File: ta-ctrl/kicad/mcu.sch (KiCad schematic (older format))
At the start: 5 parts

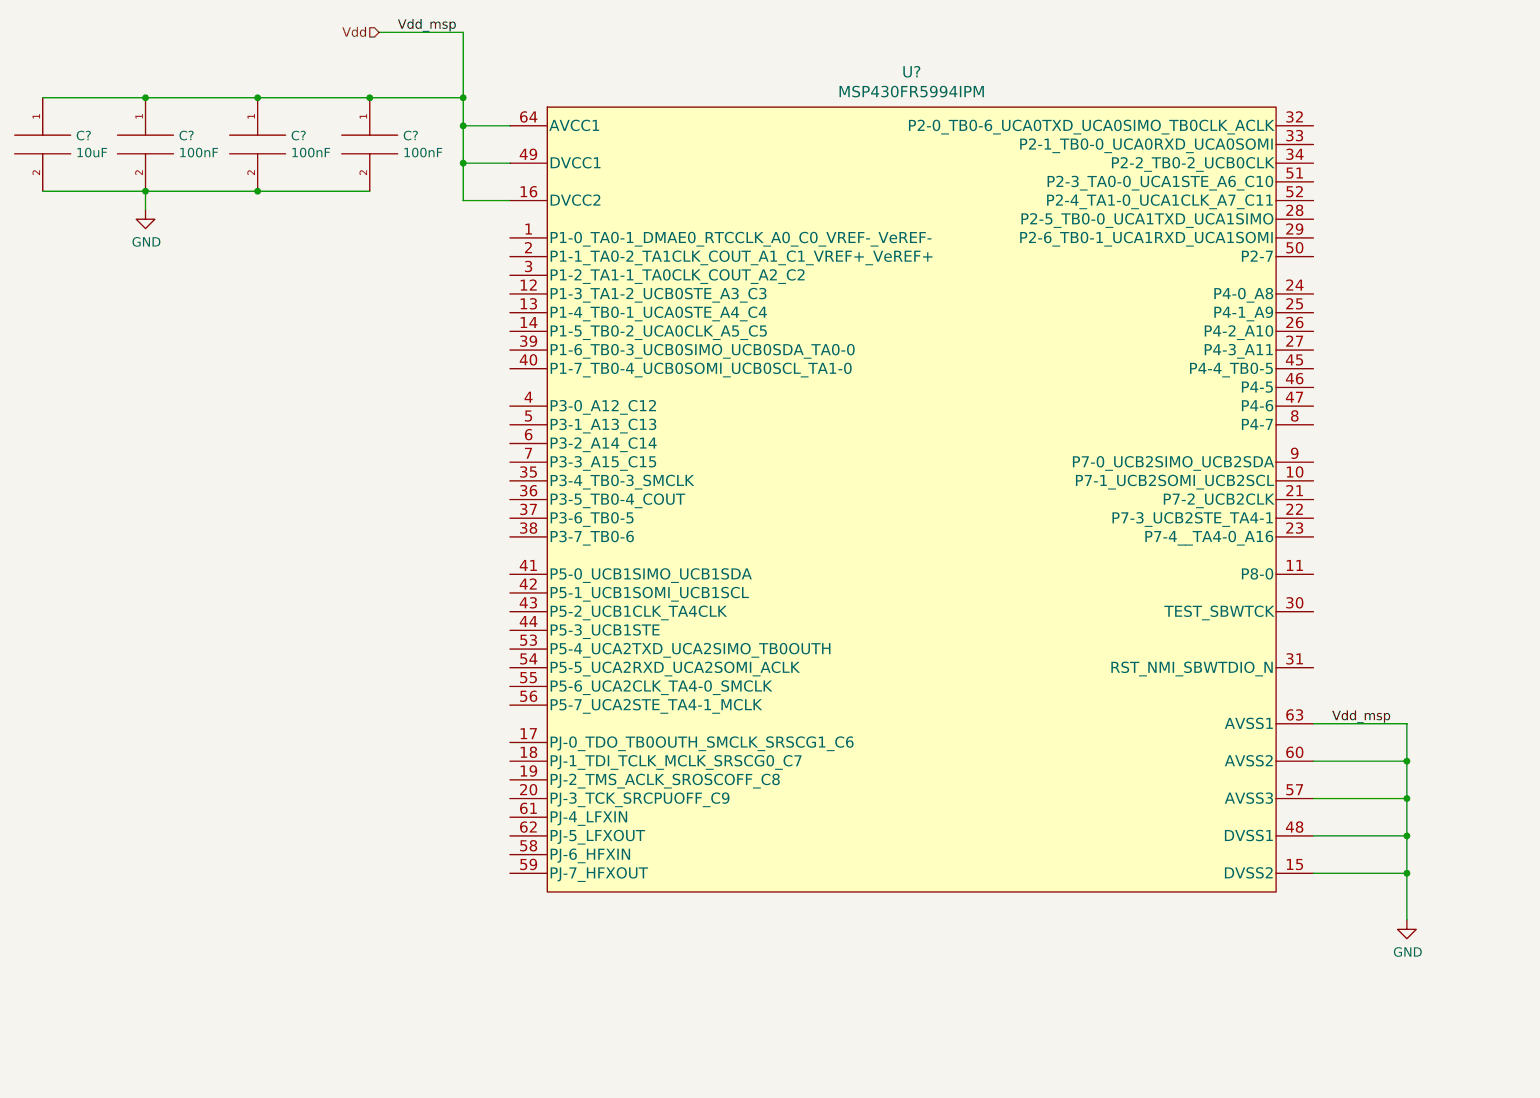
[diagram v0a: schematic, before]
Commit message: Added initial pin assignments
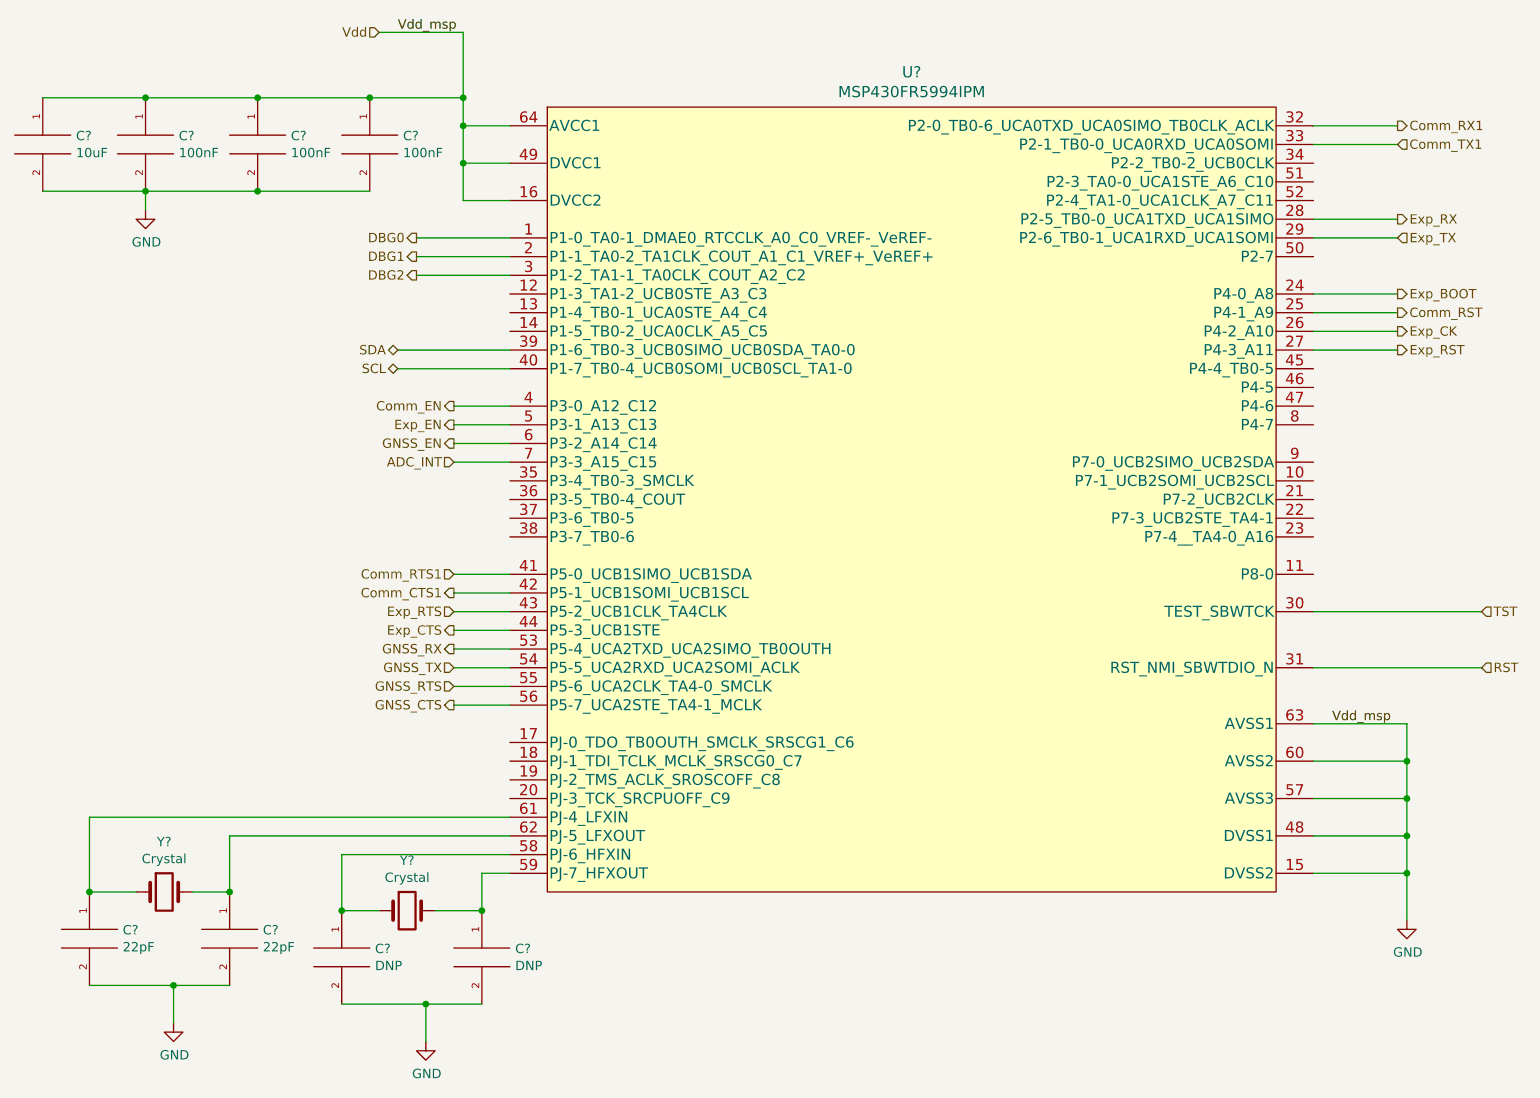
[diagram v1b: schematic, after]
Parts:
- added C? (x2): 22pF, symbol pspice:C
- added C? (x2): DNP, symbol pspice:C
- added Y? (x2): Crystal, symbol Device:Crystal
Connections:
- net GND: now also C?.2, C?.2, C?.2, C?.2
- net DBG0: now reaches U?.1 (P1-0_TA0-1_DMAE0_RTCCLK_A0_C0_VREF-_VeREF-)
- net DBG1: now reaches U?.2 (P1-1_TA0-2_TA1CLK_COUT_A1_C1_VREF+_VeREF+)
- net Exp_BOOT: now reaches U?.24 (P4-0_A8)
- net Comm_RST: now reaches U?.25 (P4-1_A9)
- net Exp_CK: now reaches U?.26 (P4-2_A10)
- net Exp_RST: now reaches U?.27 (P4-3_A11)
- net Exp_RX: now reaches U?.28 (P2-5_TB0-0_UCA1TXD_UCA1SIMO)
- net Exp_TX: now reaches U?.29 (P2-6_TB0-1_UCA1RXD_UCA1SOMI)
- net DBG2: now reaches U?.3 (P1-2_TA1-1_TA0CLK_COUT_A2_C2)
- net TST: now reaches U?.30 (TEST_SBWTCK)
- net RST: now reaches U?.31 (RST_NMI_SBWTDIO_N)
- net Comm_RX1: now reaches U?.32 (P2-0_TB0-6_UCA0TXD_UCA0SIMO_TB0CLK_ACLK)
- net Comm_TX1: now reaches U?.33 (P2-1_TB0-0_UCA0RXD_UCA0SOMI)
- net SDA: now reaches U?.39 (P1-6_TB0-3_UCB0SIMO_UCB0SDA_TA0-0)
- net Comm_EN: now reaches U?.4 (P3-0_A12_C12)
- net SCL: now reaches U?.40 (P1-7_TB0-4_UCB0SOMI_UCB0SCL_TA1-0)
- net Comm_RTS1: now reaches U?.41 (P5-0_UCB1SIMO_UCB1SDA)
- net Comm_CTS1: now reaches U?.42 (P5-1_UCB1SOMI_UCB1SCL)
- net Exp_RTS: now reaches U?.43 (P5-2_UCB1CLK_TA4CLK)
- net Exp_CTS: now reaches U?.44 (P5-3_UCB1STE)
- net Exp_EN: now reaches U?.5 (P3-1_A13_C13)
- net GNSS_RX: now reaches U?.53 (P5-4_UCA2TXD_UCA2SIMO_TB0OUTH)
- net GNSS_TX: now reaches U?.54 (P5-5_UCA2RXD_UCA2SOMI_ACLK)
- net GNSS_RTS: now reaches U?.55 (P5-6_UCA2CLK_TA4-0_SMCLK)
- net GNSS_CTS: now reaches U?.56 (P5-7_UCA2STE_TA4-1_MCLK)
- net at U?.58 (PJ-6_HFXIN): now also C?.1, Y?.1
- net at U?.59 (PJ-7_HFXOUT): now also C?.1, Y?.2
- net GNSS_EN: now reaches U?.6 (P3-2_A14_C14)
- net at U?.61 (PJ-4_LFXIN): now also C?.1, Y?.1
- net at U?.62 (PJ-5_LFXOUT): now also C?.1, Y?.2
- net ADC_INT: now reaches U?.7 (P3-3_A15_C15)
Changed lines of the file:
@@
 	3100 1750 3350 1750
-Wire Wire Line
-	3100 1750 3100 1950
-Wire Wire Line
-	3100 1950 3350 1950
-Connection ~ 3100 1750
 Wire Wire Line
 	3100 1550 3100 1400
@@
 Wire Wire Line
 	850  1900 1400 1900
+$Comp
+L Device:Crystal Y?
+U 1 1 5F187D6E
+P 2800 5750
+F 0 "Y?" H 2800 6018 50  0000 C CNN
+F 1 "Crystal" H 2800 5927 50  0000 C CNN
+F 2 "" H 2800 5750 50  0001 C CNN
+F 3 "~" H 2800 5750 50  0001 C CNN
+	1    2800 5750
+	1    0    0    -1
+$EndComp
+$Comp
+L Device:Crystal Y?
+U 1 1 5F18970C
+P 1500 5650
+F 0 "Y?" H 1500 5918 50  0000 C CNN
+F 1 "Crystal" H 1500 5827 50  0000 C CNN
+F 2 "" H 1500 5650 50  0001 C CNN
+F 3 "~" H 1500 5650 50  0001 C CNN
+	1    1500 5650
+	1    0    0    -1
+$EndComp
+$Comp
+L pspice:C C?
+U 1 1 5F189B82
+P 1850 5900
+F 0 "C?" H 2028 5946 50  0000 L CNN
+F 1 "22pF" H 2028 5855 50  0000 L CNN
+F 2 "" H 1850 5900 50  0001 C CNN
+F 3 "~" H 1850 5900 50  0001 C CNN
+	1    1850 5900
+	1    0    0    -1
+$EndComp
+$Comp
+L pspice:C C?
+U 1 1 5F18B631
+P 1100 5900
+F 0 "C?" H 1278 5946 50  0000 L CNN
+F 1 "22pF" H 1278 5855 50  0000 L CNN
+F 2 "" H 1100 5900 50  0001 C CNN
+F 3 "~" H 1100 5900 50  0001 C CNN
+	1    1100 5900
+	1    0    0    -1
+$EndComp
+$Comp
+L power:GND #PWR?
+U 1 1 5F18C345
+P 1550 6350
+F 0 "#PWR?" H 1550 6100 50  0001 C CNN
+F 1 "GND" H 1555 6177 50  0000 C CNN
+F 2 "" H 1550 6350 50  0001 C CNN
+F 3 "" H 1550 6350 50  0001 C CNN
+	1    1550 6350
+	1    0    0    -1
+$EndComp
+Wire Wire Line
+	1100 6150 1550 6150
+Wire Wire Line
+	1550 6150 1550 6350
+Connection ~ 1550 6150
+Wire Wire Line
+	1550 6150 1850 6150
+Wire Wire Line
+	1100 5650 1350 5650
+Wire Wire Line
+	1650 5650 1850 5650
+Wire Wire Line
+	1850 5650 1850 5350
+Wire Wire Line
+	1850 5350 3350 5350
+Connection ~ 1850 5650
+Wire Wire Line
+	1100 5650 1100 5250
+Wire Wire Line
+	1100 5250 3350 5250
+Connection ~ 1100 5650
+$Comp
+L pspice:C C?
+U 1 1 5F191540
+P 3200 6000
+F 0 "C?" H 3378 6046 50  0000 L CNN
+F 1 "DNP" H 3378 5955 50  0000 L CNN
+F 2 "" H 3200 6000 50  0001 C CNN
+F 3 "~" H 3200 6000 50  0001 C CNN
+	1    3200 6000
+	1    0    0    -1
+$EndComp
+$Comp
+L pspice:C C?
+U 1 1 5F191546
+P 2450 6000
+F 0 "C?" H 2628 6046 50  0000 L CNN
+F 1 "DNP" H 2628 5955 50  0000 L CNN
+F 2 "" H 2450 6000 50  0001 C CNN
+F 3 "~" H 2450 6000 50  0001 C CNN
+	1    2450 6000
+	1    0    0    -1
+$EndComp
+$Comp
+L power:GND #PWR?
+U 1 1 5F19154C
+P 2900 6450
+F 0 "#PWR?" H 2900 6200 50  0001 C CNN
+F 1 "GND" H 2905 6277 50  0000 C CNN
+F 2 "" H 2900 6450 50  0001 C CNN
+F 3 "" H 2900 6450 50  0001 C CNN
+	1    2900 6450
+	1    0    0    -1
+$EndComp
+Wire Wire Line
+	2450 6250 2900 6250
+Wire Wire Line
+	2900 6250 2900 6450
+Connection ~ 2900 6250
+Wire Wire Line
+	2900 6250 3200 6250
+Wire Wire Line
+	2450 5750 2650 5750
+Wire Wire Line
+	2950 5750 3200 5750
+Wire Wire Line
+	2450 5750 2450 5450
+Wire Wire Line
+	2450 5450 3350 5450
+Connection ~ 2450 5750
+Wire Wire Line
+	3200 5750 3200 5550
+Wire Wire Line
+	3200 5550 3350 5550
+Connection ~ 3200 5750
+Text HLabel 8550 4150 2    50   Input ~ 0
+TST
+Text HLabel 8550 4450 2    50   Input ~ 0
+RST
+Wire Wire Line
+	7650 4450 8550 4450
+Wire Wire Line
+	7650 4150 8550 4150
+Text HLabel 8100 1550 2    50   Output ~ 0
+Comm_RX1
+Text HLabel 8100 1650 2    50   Input ~ 0
+Comm_TX1
+Text HLabel 8100 2050 2    50   Output ~ 0
+Exp_RX
+Text HLabel 8100 2150 2    50   Input ~ 0
+Exp_TX
+Text HLabel 3050 4250 0    50   Output ~ 0
+Exp_CTS
+Text HLabel 3050 4150 0    50   Input ~ 0
+Exp_RTS
+Text HLabel 3050 4350 0    50   Output ~ 0
+GNSS_RX
+Text HLabel 3050 4450 0    50   Input ~ 0
+GNSS_TX
+Text HLabel 3050 4650 0    50   Output ~ 0
+GNSS_CTS
+Text HLabel 3050 4550 0    50   Input ~ 0
+GNSS_RTS
+Text HLabel 2750 2750 0    50   BiDi ~ 0
+SDA
+Text HLabel 2750 2850 0    50   BiDi ~ 0
+SCL
+Wire Wire Line
+	2750 2850 3350 2850
+Wire Wire Line
+	2750 2750 3350 2750
+Wire Wire Line
+	7650 1550 8100 1550
+Wire Wire Line
+	7650 1650 8100 1650
+Wire Wire Line
+	7650 2050 8100 2050
+Wire Wire Line
+	7650 2150 8100 2150
+Wire Wire Line
+	3050 4350 3350 4350
+Wire Wire Line
+	3350 4450 3050 4450
+Text HLabel 3050 4050 0    50   Output ~ 0
+Comm_CTS1
+Text HLabel 3050 3950 0    50   Input ~ 0
+Comm_RTS1
+Wire Wire Line
+	3050 4550 3350 4550
+Wire Wire Line
+	3050 4650 3350 4650
+Wire Wire Line
+	3050 3950 3350 3950
+Wire Wire Line
+	3050 4050 3350 4050
+Wire Wire Line
+	3050 4150 3350 4150
+Wire Wire Line
+	3050 4250 3350 4250
+Text HLabel 3050 3050 0    50   Output ~ 0
+Comm_EN
+Text HLabel 3050 3150 0    50   Output ~ 0
+Exp_EN
+Text HLabel 3050 3250 0    50   Output ~ 0
+GNSS_EN
+Wire Wire Line
+	3050 3250 3350 3250
+Wire Wire Line
+	3050 3150 3350 3150
+Wire Wire Line
+	3050 3050 3350 3050
+Text HLabel 3050 3350 0    50   Input ~ 0
+ADC_INT
+Wire Wire Line
+	3050 3350 3350 3350
+Text HLabel 2850 2250 0    50   Output ~ 0
+DBG1
+Text HLabel 2850 2350 0    50   Output ~ 0
+DBG2
+Wire Wire Line
+	3350 2250 2850 2250
+Wire Wire Line
+	3350 2350 2850 2350
+Connection ~ 3100 1750
+Wire Wire Line
+	3350 2150 2850 2150
+Text HLabel 2850 2150 0    50   Output ~ 0
+DBG0
+Wire Wire Line
+	3100 1950 3350 1950
+Wire Wire Line
+	3100 1750 3100 1950
+Text HLabel 8100 2450 2    50   Output ~ 0
+Exp_BOOT
+Text HLabel 8100 2550 2    50   Output ~ 0
+Comm_RST
+Wire Wire Line
+	7650 2450 8100 2450
+Wire Wire Line
+	7650 2550 8100 2550
+Text HLabel 8100 2650 2    50   Output ~ 0
+Exp_CK
+Text HLabel 8100 2750 2    50   Output ~ 0
+Exp_RST
+Wire Wire Line
+	7650 2650 8100 2650
+Wire Wire Line
+	7650 2750 8100 2750
 $EndSCHEMATC

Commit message: finalized connections to MCU
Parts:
- gave numbers to parts that had none: 11
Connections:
- net DRDY_M: now reaches U6.17 (PJ-0_TDO_TB0OUTH_SMCLK_SRSCG1_C6)
- net INT_M: now reaches U6.18 (PJ-1_TDI_TCLK_MCLK_SRSCG0_C7)
- net INT_AG: now reaches U6.19 (PJ-2_TMS_ACLK_SROSCOFF_C8)
- net DEN_AG: now reaches U6.20 (PJ-3_TCK_SRCPUOFF_C9)
- net GNSS_CTS renamed GNSS_nRST
- net GNSS_RTS renamed GNSS_PPS
- no-connect marks 0 -> 21
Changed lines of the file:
@@
 $Descr A4 11693 8268
 encoding utf-8
-Sheet 2 3
+Sheet 3 3
 Title ""
 Date ""
@@
 $EndDescr
 $Comp
-L ta-ctrl:MSP430FR5994IPM U?
+L ta-ctrl:MSP430FR5994IPM U6
 U 1 1 5F18628C
 P 5700 3550
-F 0 "U?" H 5500 5837 60  0000 C CNN
+F 0 "U6" H 5500 5837 60  0000 C CNN
 F 1 "MSP430FR5994IPM" H 5500 5731 60  0000 C CNN
 F 2 "PM0064A_N" H 5700 3490 60  0001 C CNN
@@
 Vdd_msp
 $Comp
-L power:GND #PWR?
+L power:GND #PWR021
 U 1 1 5F18B739
 P 8150 5800
-F 0 "#PWR?" H 8150 5550 50  0001 C CNN
+F 0 "#PWR021" H 8150 5550 50  0001 C CNN
 F 1 "GND" H 8155 5627 50  0000 C CNN
 F 2 "" H 8150 5800 50  0001 C CNN
@@
 Connection ~ 8150 5550
 $Comp
-L pspice:C C?
+L pspice:C C8
 U 1 1 5F18BB04
 P 1400 1650
-F 0 "C?" H 1578 1696 50  0000 L CNN
+F 0 "C8" H 1578 1696 50  0000 L CNN
 F 1 "100nF" H 1578 1605 50  0000 L CNN
 F 2 "" H 1400 1650 50  0001 C CNN
@@
 $EndComp
 $Comp
-L pspice:C C?
+L pspice:C C10
 U 1 1 5F18C90D
 P 2000 1650
-F 0 "C?" H 2178 1696 50  0000 L CNN
+F 0 "C10" H 2178 1696 50  0000 L CNN
 F 1 "100nF" H 2178 1605 50  0000 L CNN
 F 2 "" H 2000 1650 50  0001 C CNN
@@
 $EndComp
 $Comp
-L pspice:C C?
+L pspice:C C12
 U 1 1 5F18CCD0
 P 2600 1650
-F 0 "C?" H 2778 1696 50  0000 L CNN
+F 0 "C12" H 2778 1696 50  0000 L CNN
 F 1 "100nF" H 2778 1605 50  0000 L CNN
 F 2 "" H 2600 1650 50  0001 C CNN
@@
 $EndComp
 $Comp
-L power:GND #PWR?
+L power:GND #PWR018
 U 1 1 5F18D1CF
 P 1400 2000
-F 0 "#PWR?" H 1400 1750 50  0001 C CNN
+F 0 "#PWR018" H 1400 1750 50  0001 C CNN
 F 1 "GND" H 1405 1827 50  0000 C CNN
 F 2 "" H 1400 2000 50  0001 C CNN
@@
 	2600 1400 3100 1400
 $Comp
-L pspice:C C?
+L pspice:C C6
 U 1 1 5F18EA80
 P 850 1650
-F 0 "C?" H 1028 1696 50  0000 L CNN
+F 0 "C6" H 1028 1696 50  0000 L CNN
 F 1 "10uF" H 1028 1605 50  0000 L CNN
 F 2 "" H 850 1650 50  0001 C CNN
@@
 	850  1900 1400 1900
 $Comp
-L Device:Crystal Y?
+L Device:Crystal Y2
 U 1 1 5F187D6E
 P 2800 5750
-F 0 "Y?" H 2800 6018 50  0000 C CNN
+F 0 "Y2" H 2800 6018 50  0000 C CNN
 F 1 "Crystal" H 2800 5927 50  0000 C CNN
 F 2 "" H 2800 5750 50  0001 C CNN
@@
 $EndComp
 $Comp
-L Device:Crystal Y?
+L Device:Crystal Y1
 U 1 1 5F18970C
 P 1500 5650
-F 0 "Y?" H 1500 5918 50  0000 C CNN
+F 0 "Y1" H 1500 5918 50  0000 C CNN
 F 1 "Crystal" H 1500 5827 50  0000 C CNN
 F 2 "" H 1500 5650 50  0001 C CNN
@@
 $EndComp
 $Comp
-L pspice:C C?
+L pspice:C C9
 U 1 1 5F189B82
 P 1850 5900
-F 0 "C?" H 2028 5946 50  0000 L CNN
+F 0 "C9" H 2028 5946 50  0000 L CNN
 F 1 "22pF" H 2028 5855 50  0000 L CNN
 F 2 "" H 1850 5900 50  0001 C CNN
@@
 $EndComp
 $Comp
-L pspice:C C?
+L pspice:C C7
 U 1 1 5F18B631
 P 1100 5900
-F 0 "C?" H 1278 5946 50  0000 L CNN
+F 0 "C7" H 1278 5946 50  0000 L CNN
 F 1 "22pF" H 1278 5855 50  0000 L CNN
 F 2 "" H 1100 5900 50  0001 C CNN
@@
 $EndComp
 $Comp
-L power:GND #PWR?
+L power:GND #PWR019
 U 1 1 5F18C345
 P 1550 6350
-F 0 "#PWR?" H 1550 6100 50  0001 C CNN
+F 0 "#PWR019" H 1550 6100 50  0001 C CNN
 F 1 "GND" H 1555 6177 50  0000 C CNN
 F 2 "" H 1550 6350 50  0001 C CNN
@@
 Connection ~ 1100 5650
 $Comp
-L pspice:C C?
+L pspice:C C13
 U 1 1 5F191540
 P 3200 6000
-F 0 "C?" H 3378 6046 50  0000 L CNN
+F 0 "C13" H 3378 6046 50  0000 L CNN
 F 1 "DNP" H 3378 5955 50  0000 L CNN
 F 2 "" H 3200 6000 50  0001 C CNN
@@
 $EndComp
 $Comp
-L pspice:C C?
+L pspice:C C11
 U 1 1 5F191546
 P 2450 6000
-F 0 "C?" H 2628 6046 50  0000 L CNN
+F 0 "C11" H 2628 6046 50  0000 L CNN
 F 1 "DNP" H 2628 5955 50  0000 L CNN
 F 2 "" H 2450 6000 50  0001 C CNN
@@
 $EndComp
 $Comp
-L power:GND #PWR?
+L power:GND #PWR020
 U 1 1 5F19154C
 P 2900 6450
-F 0 "#PWR?" H 2900 6200 50  0001 C CNN
+F 0 "#PWR020" H 2900 6200 50  0001 C CNN
 F 1 "GND" H 2905 6277 50  0000 C CNN
 F 2 "" H 2900 6450 50  0001 C CNN
@@
 Text HLabel 3050 4250 0    50   Output ~ 0
 Exp_CTS
-Text HLabel 3050 4150 0    50   Input ~ 0
-Exp_RTS
 Text HLabel 3050 4350 0    50   Output ~ 0
 GNSS_RX
@@
 GNSS_TX
 Text HLabel 3050 4650 0    50   Output ~ 0
-GNSS_CTS
+GNSS_nRST
 Text HLabel 3050 4550 0    50   Input ~ 0
-GNSS_RTS
+GNSS_PPS
 Text HLabel 2750 2750 0    50   BiDi ~ 0
 SDA
@@
 Wire Wire Line
 	3350 4450 3050 4450
-Text HLabel 3050 4050 0    50   Output ~ 0
-Comm_CTS1
-Text HLabel 3050 3950 0    50   Input ~ 0
-Comm_RTS1
 Wire Wire Line
 	3050 4550 3350 4550
@@
 Wire Wire Line
 	7650 2750 8100 2750
+Text HLabel 3050 4850 0    50   Input ~ 0
+DRDY_M
+Text HLabel 3050 4950 0    50   Input ~ 0
+INT_M
+Text HLabel 3050 5050 0    50   Input ~ 0
+INT_AG
+Text HLabel 3050 5150 0    50   Input ~ 0
+DEN_AG
+Wire Wire Line
+	3050 5150 3350 5150
+Wire Wire Line
+	3050 5050 3350 5050
+Wire Wire Line
+	3050 4950 3350 4950
+Wire Wire Line
+	3050 4850 3350 4850
+Text HLabel 3050 4150 0    50   Input ~ 0
+Exp_RTS
+Text HLabel 3050 4050 0    50   Output ~ 0
+Comm_CTS1
+Text HLabel 3050 3950 0    50   Input ~ 0
+Comm_RTS1
+NoConn ~ 3200 3450
+NoConn ~ 3200 3550
+NoConn ~ 3200 3650
+NoConn ~ 3200 3750
+Wire Wire Line
+	3200 3450 3350 3450
+Wire Wire Line
+	3200 3550 3350 3550
+Wire Wire Line
+	3200 3650 3350 3650
+Wire Wire Line
+	3200 3750 3350 3750
+NoConn ~ 3250 2450
+NoConn ~ 3250 2550
+NoConn ~ 3250 2650
+Wire Wire Line
+	3250 2450 3350 2450
+Wire Wire Line
+	3250 2550 3350 2550
+Wire Wire Line
+	3250 2650 3350 2650
+NoConn ~ 7800 1750
+NoConn ~ 7800 1850
+NoConn ~ 7800 1950
+Wire Wire Line
+	7650 1750 7800 1750
+Wire Wire Line
+	7650 1850 7800 1850
+Wire Wire Line
+	7650 1950 7800 1950
+NoConn ~ 7800 2250
+Wire Wire Line
+	7650 2250 7800 2250
+NoConn ~ 7800 2850
+NoConn ~ 7800 2950
+NoConn ~ 7800 3050
+NoConn ~ 7800 3150
+Wire Wire Line
+	7650 2850 7800 2850
+Wire Wire Line
+	7650 2950 7800 2950
+Wire Wire Line
+	7650 3050 7800 3050
+Wire Wire Line
+	7650 3150 7800 3150
+NoConn ~ 7800 3350
+NoConn ~ 7800 3450
+NoConn ~ 7800 3550
+NoConn ~ 7800 3650
+NoConn ~ 7800 3750
+Wire Wire Line
+	7650 3350 7800 3350
+Wire Wire Line
+	7650 3450 7800 3450
+Wire Wire Line
+	7650 3550 7800 3550
+Wire Wire Line
+	7650 3650 7800 3650
+Wire Wire Line
+	7650 3750 7800 3750
+NoConn ~ 7800 3950
+Wire Wire Line
+	7650 3950 7800 3950
 $EndSCHEMATC

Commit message: more footprints, changed symbol library path
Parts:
- U6: footprint PM0064A_N -> ta-ctrl:MSP430FR5994IPM
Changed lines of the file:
@@
 F 0 "U6" H 5500 5837 60  0000 C CNN
 F 1 "MSP430FR5994IPM" H 5500 5731 60  0000 C CNN
-F 2 "PM0064A_N" H 5700 3490 60  0001 C CNN
+F 2 "ta-ctrl:MSP430FR5994IPM" H 5700 3490 60  0001 C CNN
 F 3 "" H 5700 3550 60  0000 C CNN
 	1    5700 3550
